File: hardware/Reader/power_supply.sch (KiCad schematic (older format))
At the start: 3 parts

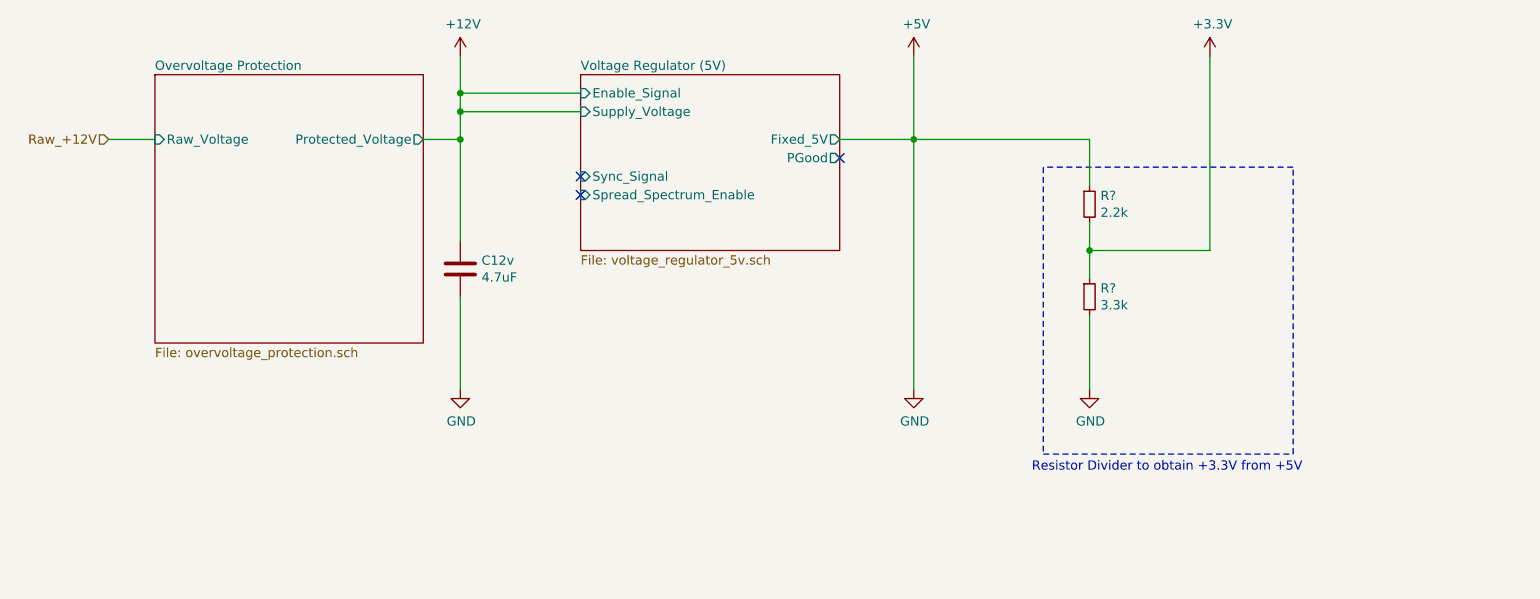
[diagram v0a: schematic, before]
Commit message: Completed schematics for reader
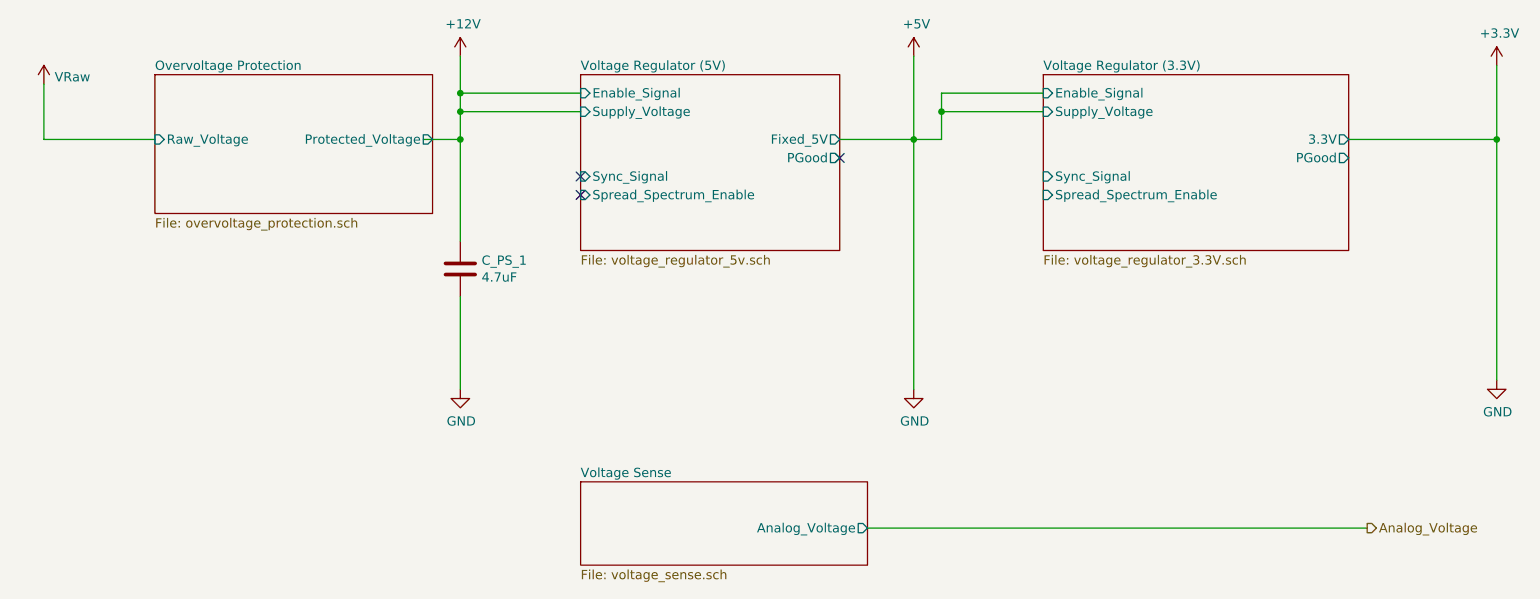
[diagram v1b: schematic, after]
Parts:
- removed R?: 2.2k, symbol Device:R_Small
- removed R?: 3.3k, symbol Device:R_Small
- C_PS_1: renamed from C12v; footprint (none) -> footprints:C1206C475K3RACAUTO; Part Name (none) -> C1206C475K3RACAUTO
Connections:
- net labels added: Analog_Voltage, VRaw
- net labels removed: Raw_+12V
- wire segments 19 -> 22
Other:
- note removed: "Resistor Divider to obtain +3.3V from +5V"
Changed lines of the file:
@@
 $Descr USLetter 11000 8500
 encoding utf-8
-Sheet 3 9
-Title ""
-Date "2020-10-18"
+Sheet 2 17
+Title "CANnect Reader | Power Supply"
+Date "2020-10-20"
 Rev "0.0.1"
 Comp "CANtech"
-Comment1 ""
+Comment1 "Created by Choong Jin Ng | jin8383@gmail.com"
 Comment2 ""
 Comment3 ""
-Comment4 ""
+Comment4 "Component Identifier: PS"
 $EndDescr
-Text HLabel 1450 1850 0    50   Input ~ 0
-Raw_+12V
-Wire Wire Line
-	1450 1850 1700 1850
 $Comp
 L power:GND #PWR0109
@@
 	3150 1850 3350 1850
 $Comp
-L Device:C C12v
+L Device:C C_PS_1
 U 1 1 5F9D0FD9
 P 3350 2550
-F 0 "C12v" H 3465 2596 50  0000 L CNN
+F 0 "C_PS_1" H 3465 2596 50  0000 L CNN
 F 1 "4.7uF" H 3465 2505 50  0000 L CNN
-F 2 "" H 3388 2400 50  0001 C CNN
-F 3 "~" H 3350 2550 50  0001 C CNN
+F 2 "footprints:C1206C475K3RACAUTO" H 3388 2400 50  0001 C CNN
+F 3 "https://api.kemet.com/component-edge/download/specsheet/C1206C475K3RACAUTO.pdf" H 3350 2550 50  0001 C CNN
+F 4 "C1206C475K3RACAUTO" H 3350 2550 50  0001 C CNN "Part Name"
 	1    3350 2550
 	1    0    0    -1
@@
 Connection ~ 5800 1850
 $Comp
-L Device:R_Small R?
-U 1 1 5F9FD1AC
-P 6750 2200
-F 0 "R?" H 6809 2246 50  0000 L CNN
-F 1 "2.2k" H 6809 2155 50  0000 L CNN
-F 2 "" H 6750 2200 50  0001 C CNN
-F 3 "~" H 6750 2200 50  0001 C CNN
-	1    6750 2200
+L power:+3.3V #PWR0113
+U 1 1 5F9FE7BA
+P 8950 1450
+F 0 "#PWR0113" H 8950 1300 50  0001 C CNN
+F 1 "+3.3V" H 8965 1623 50  0000 C CNN
+F 2 "" H 8950 1450 50  0001 C CNN
+F 3 "" H 8950 1450 50  0001 C CNN
+	1    8950 1450
 	1    0    0    -1
 $EndComp
-$Comp
-L Device:R_Small R?
-U 1 1 5F9FD5A4
-P 6750 2700
-F 0 "R?" H 6809 2746 50  0000 L CNN
-F 1 "3.3k" H 6809 2655 50  0000 L CNN
-F 2 "" H 6750 2700 50  0001 C CNN
-F 3 "~" H 6750 2700 50  0001 C CNN
-	1    6750 2700
-	1    0    0    -1
-$EndComp
-$Comp
-L power:GND #PWR0112
-U 1 1 5F9FDC3A
-P 6750 3200
-F 0 "#PWR0112" H 6750 2950 50  0001 C CNN
-F 1 "GND" H 6755 3027 50  0000 C CNN
-F 2 "" H 6750 3200 50  0001 C CNN
-F 3 "" H 6750 3200 50  0001 C CNN
-	1    6750 3200
-	1    0    0    -1
-$EndComp
-Wire Wire Line
-	6750 2800 6750 3200
-Wire Wire Line
-	5800 1850 6750 1850
-Wire Wire Line
-	6750 1850 6750 2100
-Wire Wire Line
-	6750 2300 6750 2450
-$Comp
-L power:+3.3V #PWR0113
-U 1 1 5F9FE7BA
-P 7400 1400
-F 0 "#PWR0113" H 7400 1250 50  0001 C CNN
-F 1 "+3.3V" H 7415 1573 50  0000 C CNN
-F 2 "" H 7400 1400 50  0001 C CNN
-F 3 "" H 7400 1400 50  0001 C CNN
-	1    7400 1400
-	1    0    0    -1
-$EndComp
-Wire Wire Line
-	6750 2450 7400 2450
-Wire Wire Line
-	7400 2450 7400 1400
-Connection ~ 6750 2450
-Wire Wire Line
-	6750 2450 6750 2600
-Wire Notes Line
-	6500 3550 7850 3550
-Wire Notes Line
-	7850 3550 7850 2000
-Wire Notes Line
-	7850 2000 6500 2000
-Wire Notes Line
-	6500 2000 6500 3550
-Text Notes 7900 3650 2    50   ~ 0
-Resistor Divider to obtain +3.3V from +5V
 $Sheet
-S 1700 1500 1450 1450
+S 1700 1500 1500 750
 U 5F9AE5F2
 F0 "Overvoltage Protection" 50
 F1 "overvoltage_protection.sch" 50
 F2 "Raw_Voltage" I L 1700 1850 50
-F3 "Protected_Voltage" O R 3150 1850 50
+F3 "Protected_Voltage" O R 3200 1850 50
 $EndSheet
 Wire Wire Line
@@
 	3350 1700 3350 1850
 $Comp
-L power:+12V #PWR?
+L power:+12V #PWR0121
 U 1 1 5FA66599
 P 3350 1400
-F 0 "#PWR?" H 3350 1250 50  0001 C CNN
+F 0 "#PWR0121" H 3350 1250 50  0001 C CNN
 F 1 "+12V" H 3365 1573 50  0000 C CNN
 F 2 "" H 3350 1400 50  0001 C CNN
@@
 	3350 1600 3350 1400
 Connection ~ 3350 1600
+$Comp
+L CANtech:VRaw #V0102
+U 1 1 5FD5C101
+P 1100 1500
+F 0 "#V0102" H 1100 1500 50  0001 C CNN
+F 1 "VRaw" H 1158 1487 50  0000 L CNN
+F 2 "" H 1100 1500 50  0001 C CNN
+F 3 "" H 1100 1500 50  0001 C CNN
+	1    1100 1500
+	1    0    0    -1
+$EndComp
+Wire Wire Line
+	1100 1550 1100 1850
+Wire Wire Line
+	1100 1850 1700 1850
+Text HLabel 8250 3950 2    50   Output ~ 0
+Analog_Voltage
+$Sheet
+S 4000 3700 1550 450
+U 5FD5D295
+F0 "Voltage Sense" 50
+F1 "voltage_sense.sch" 50
+F2 "Analog_Voltage" O R 5550 3950 50
+$EndSheet
+$Sheet
+S 6500 1500 1650 950
+U 5FF30350
+F0 "Voltage Regulator (3.3V)" 50
+F1 "voltage_regulator_3.3V.sch" 50
+F2 "Enable_Signal" I L 6500 1600 50
+F3 "Supply_Voltage" I L 6500 1700 50
+F4 "Sync_Signal" I L 6500 2050 50
+F5 "3.3V" O R 8150 1850 50
+F6 "PGood" O R 8150 1950 50
+F7 "Spread_Spectrum_Enable" I L 6500 2150 50
+$EndSheet
+Wire Wire Line
+	5800 1850 5950 1850
+Wire Wire Line
+	5950 1850 5950 1700
+Wire Wire Line
+	5950 1600 6500 1600
+Wire Wire Line
+	6500 1700 5950 1700
+Connection ~ 5950 1700
+Wire Wire Line
+	5950 1700 5950 1600
+Wire Wire Line
+	8150 1850 8950 1850
+Wire Wire Line
+	8950 1850 8950 1450
+$Comp
+L power:GND #PWR0106
+U 1 1 5FF439F1
+P 8950 3150
+F 0 "#PWR0106" H 8950 2900 50  0001 C CNN
+F 1 "GND" H 8955 2977 50  0000 C CNN
+F 2 "" H 8950 3150 50  0001 C CNN
+F 3 "" H 8950 3150 50  0001 C CNN
+	1    8950 3150
+	1    0    0    -1
+$EndComp
+Wire Wire Line
+	8950 3150 8950 1850
+Connection ~ 8950 1850
+Wire Wire Line
+	5550 3950 8250 3950
 $EndSCHEMATC

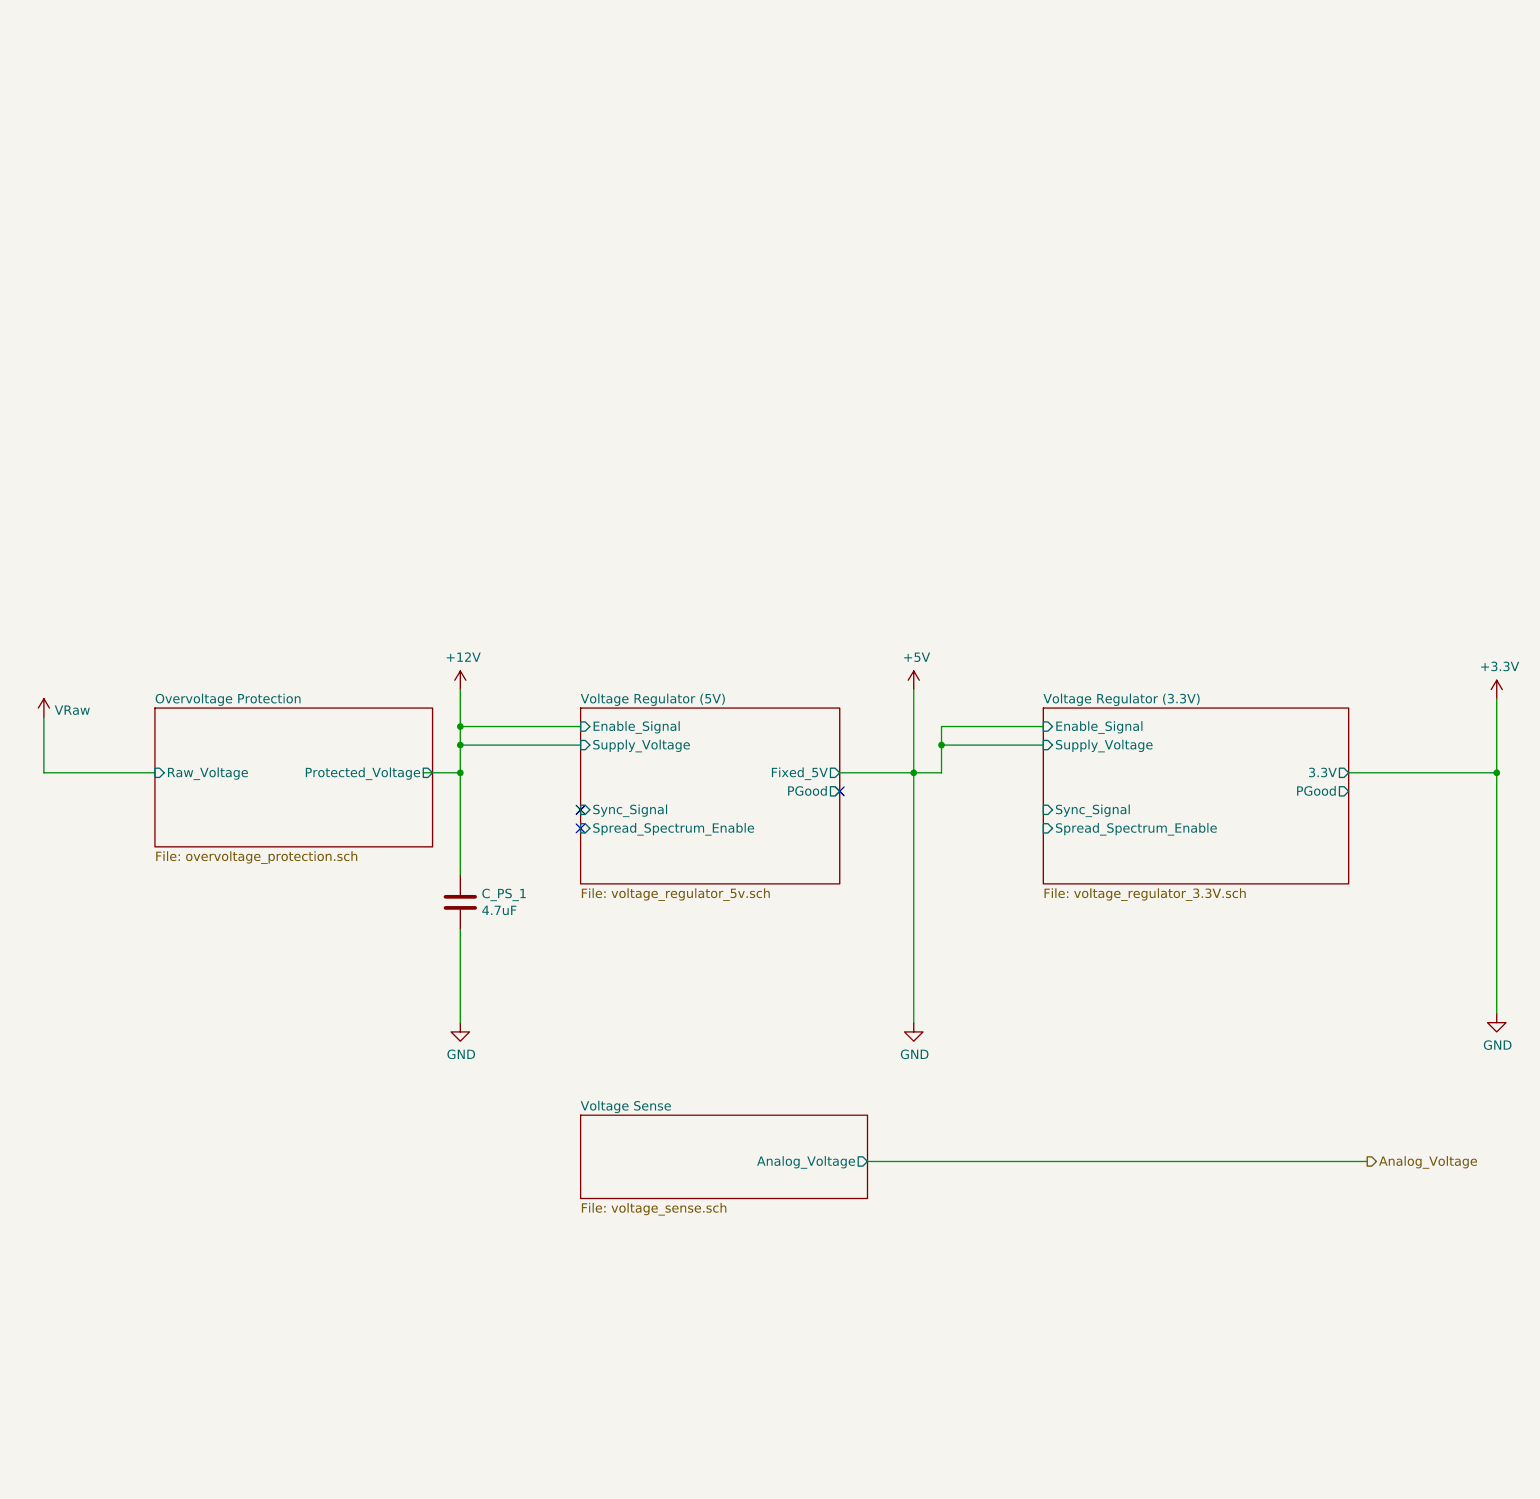
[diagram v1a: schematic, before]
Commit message: Completed Reader schematics for version 0.0.01
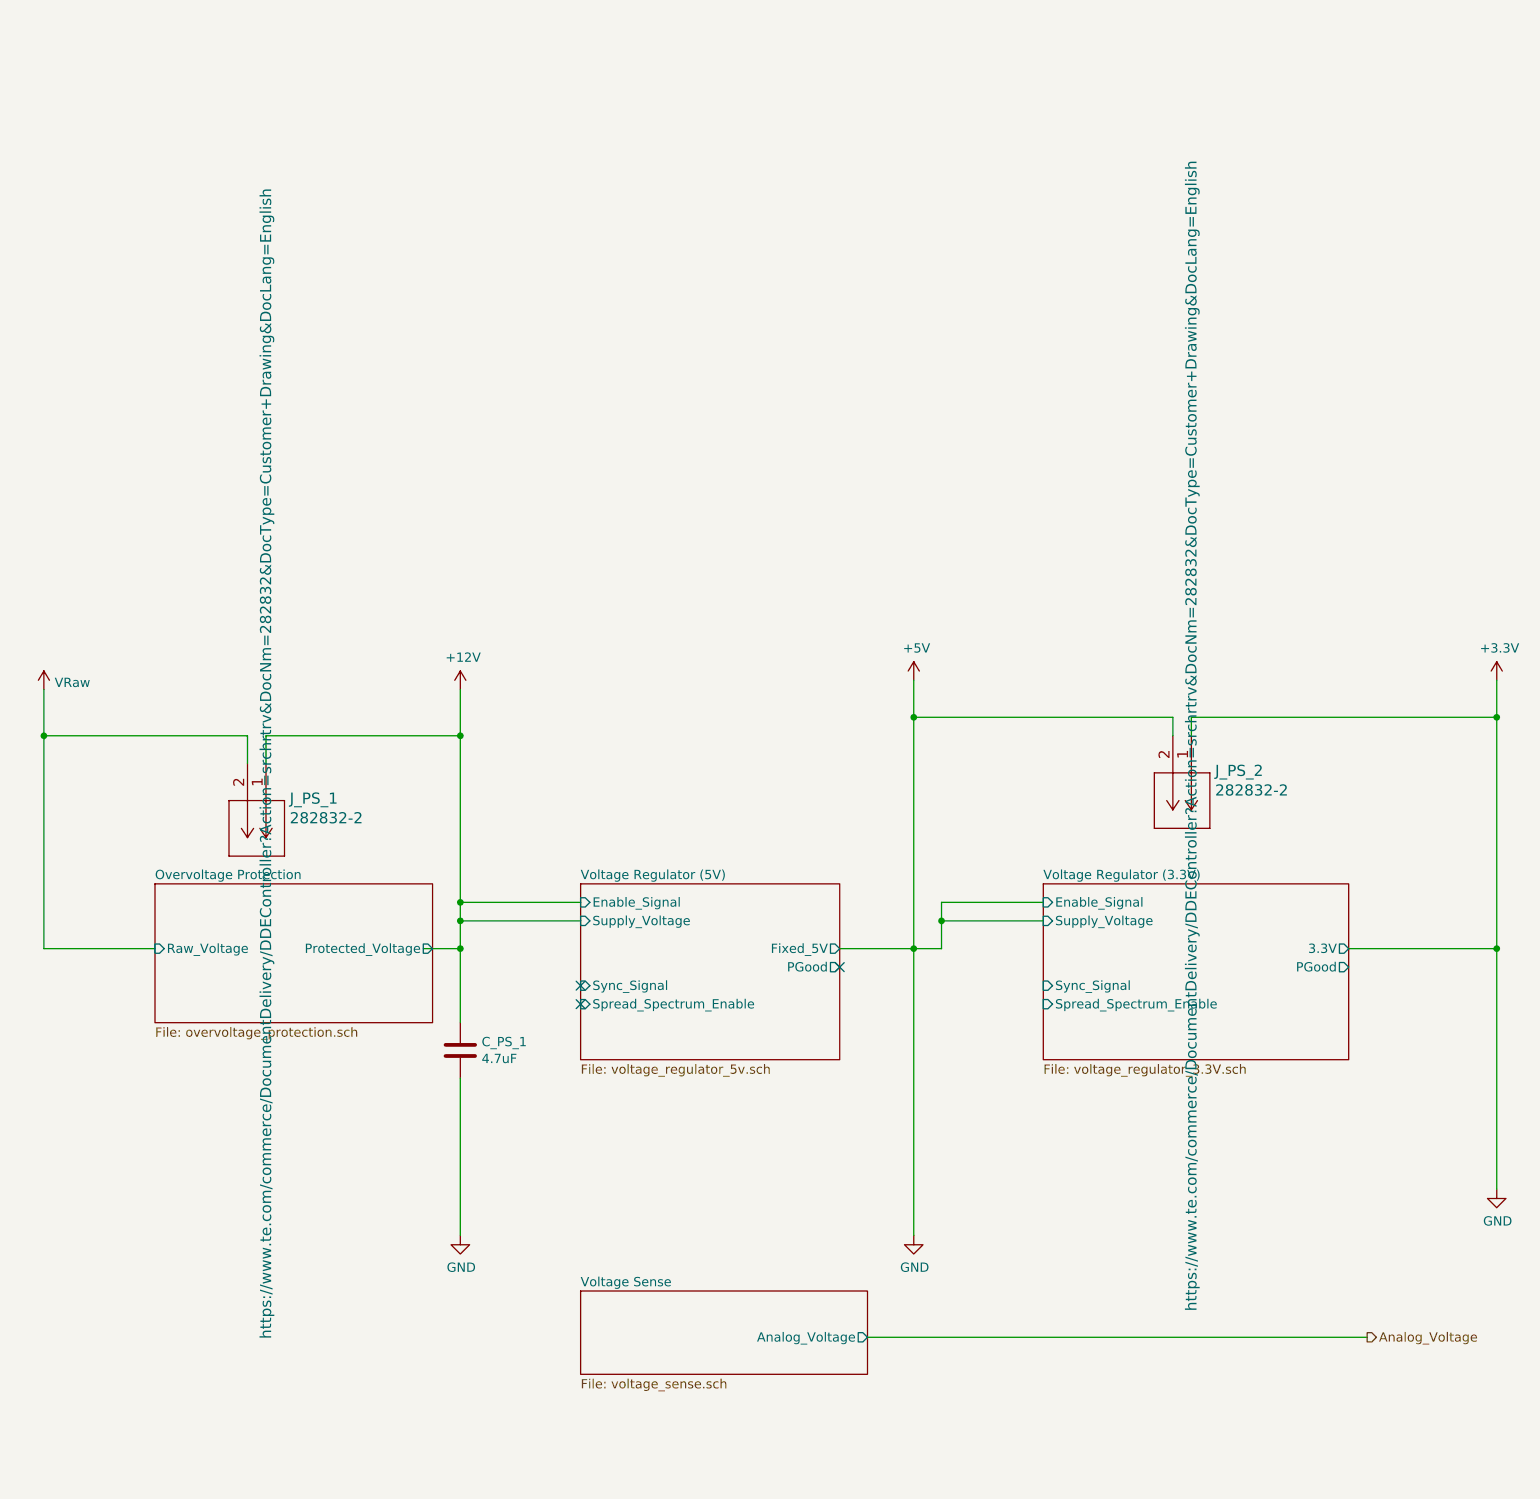
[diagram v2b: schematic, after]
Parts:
- added J_PS_1, J_PS_2: 282832-2, footprints:282832-2, symbol 2828322:282832-2
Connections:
- wire segments 22 -> 34
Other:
- moved on the sheet: C_PS_1
